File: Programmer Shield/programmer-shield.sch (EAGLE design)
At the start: 25 parts, among them T1 2N3904, T2 2N3904, T3 2N3904, T4 2N3904, U1 SPARK_CORECORE, U2 RELAYSONGLE, U3 RELAYSONGLE, U4 RELAYSONGLE, U5 RELAYSONGLE

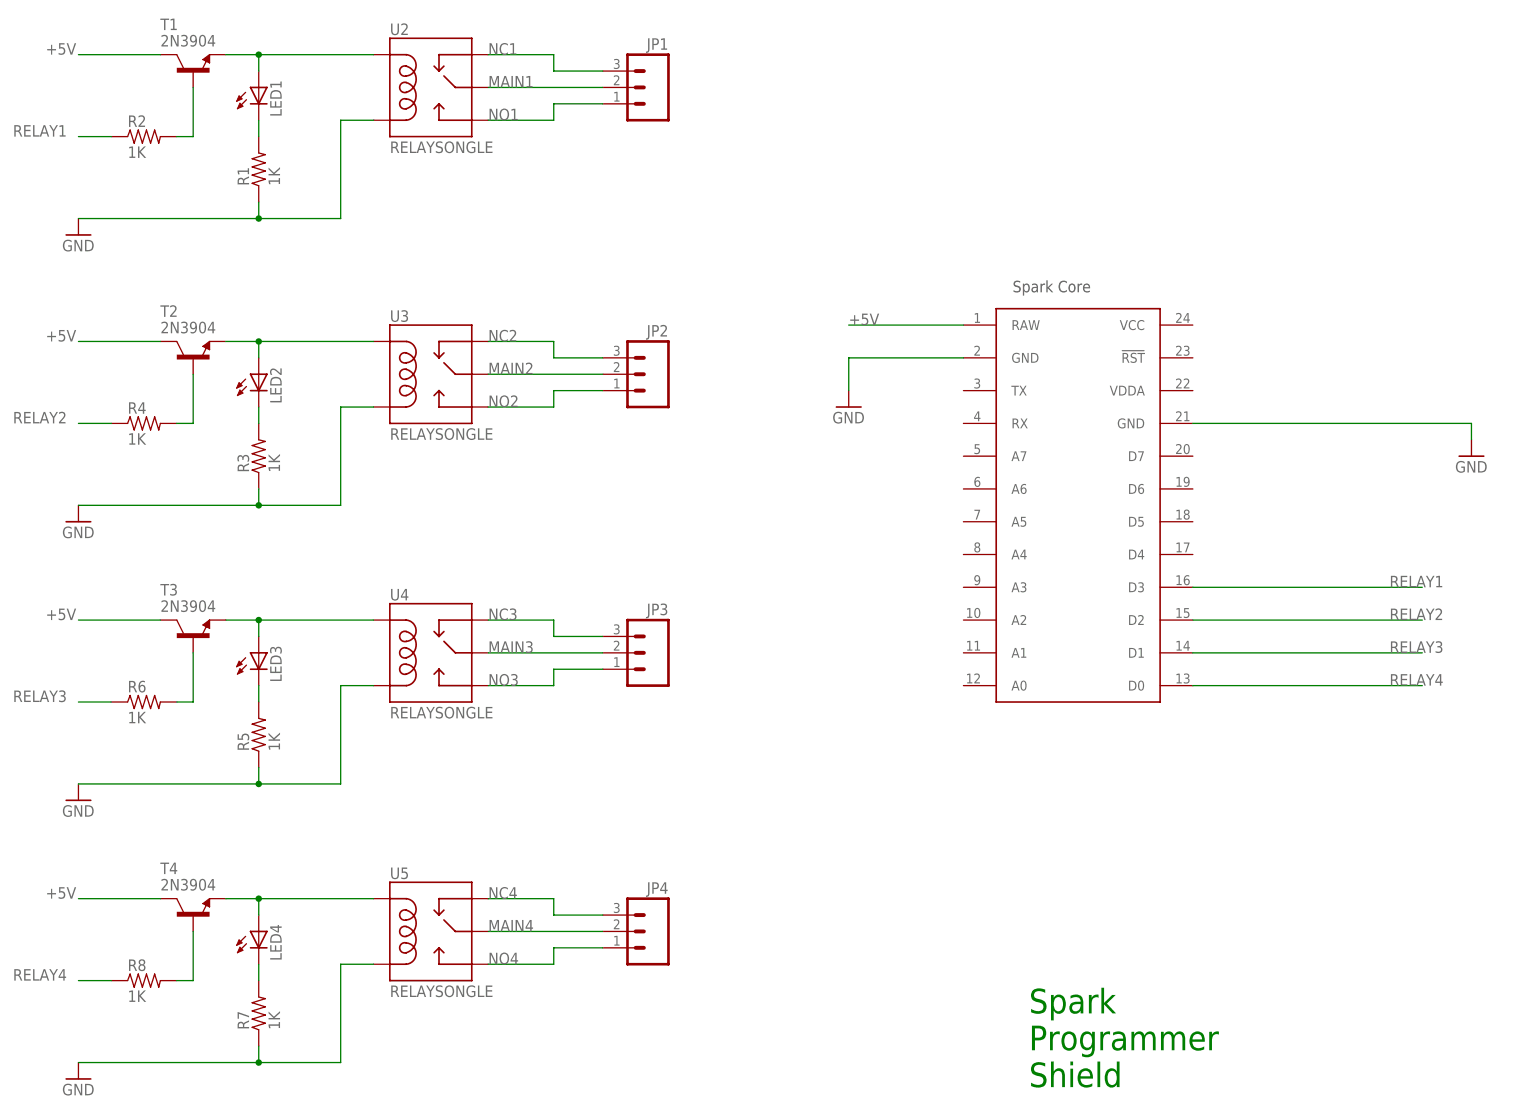
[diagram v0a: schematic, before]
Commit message: Fixed programmer shield
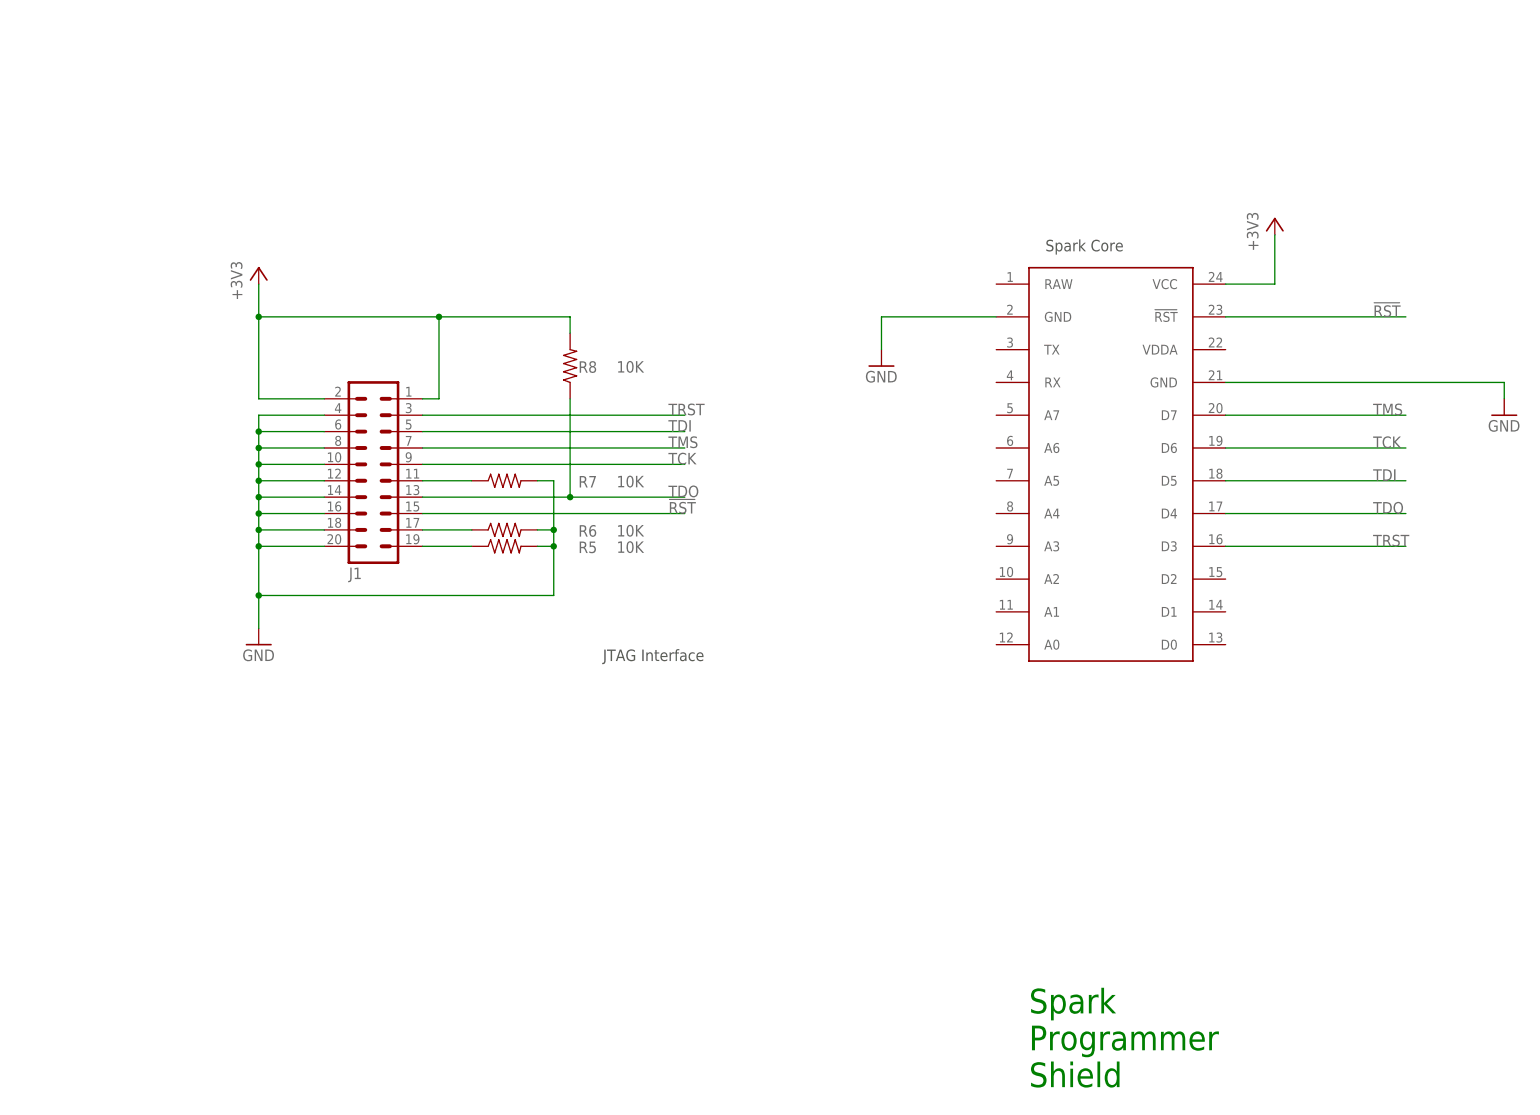
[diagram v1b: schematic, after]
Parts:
- removed JP1, JP2, JP3, JP4: (no value), SparkFun-Connectors:M03-SCREW-5MM
- removed LED1, LED2, LED3, LED4: (no value), SparkFun-LED:LED3MM
- removed R1, R2, R3, R4: 1K, SparkFun-Passives:RESISTORAXIAL-0.3
- removed T1, T2, T3, T4: 2N3904, transistor:2N3904
- removed U1: SPARK_CORECORE, Spark:SPARK_CORECORE
- removed U2, U3, U4, U5: RELAYSONGLE, Spark:RELAYSONGLE
- added J1: (no value), con-harting-ml:ML20
- added U$1: SPARK_CORECORE, Spark:SPARK_CORECORE
- R5, R6, R7, R8: value 1K -> 10K
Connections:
- removed net +5V: T1.C, T2.C, T3.C, T4.C, U1.RAW
- removed net MAIN1: JP1.2, U2.MAIN
- removed net MAIN2: JP2.2, U3.MAIN
- removed net MAIN3: JP3.2, U4.MAIN
- removed net MAIN4: JP4.2, U5.MAIN
- removed net N$1: LED1.A, T1.E, U2.COIL1
- removed net N$10: LED4.A, T4.E, U5.COIL1
- removed net N$11: R8.2, T4.B
- removed net N$12: LED4.C, R7.2
- removed net N$2: LED2.A, T2.E, U3.COIL1
- removed net N$3: R2.2, T1.B
- removed net N$4: LED1.C, R1.2
- removed net N$5: R4.2, T2.B
- removed net N$6: LED2.C, R3.2
- removed net N$7: LED3.A, T3.E, U4.COIL1
- removed net N$8: R6.2, T3.B
- removed net N$9: LED3.C, R5.2
- removed net NC1: JP1.3, U2.NC
- removed net NC2: JP2.3, U3.NC
- removed net NC3: JP3.3, U4.NC
- removed net NC4: JP4.3, U5.NC
- removed net NO1: JP1.1, U2.NO
- removed net NO2: JP2.1, U3.NO
- removed net NO3: JP3.1, U4.NO
- removed net NO4: JP4.1, U5.NO
- removed net RELAY1: R2.1, U1.D3
- removed net RELAY2: R4.1, U1.D2
- removed net RELAY3: R6.1, U1.D1
- removed net RELAY4: R8.1, U1.D0
- new net !RST: J1.15, U$1.!RST
- new net +3V3: J1.1, J1.2, R8.2, U$1.VCC
- new net N$13: J1.19, R5.1
- new net N$14: J1.17, R6.1
- new net N$15: J1.11, R7.1
- new net TCK: J1.9, U$1.D6
- new net TDI: J1.5, U$1.D5
- new net TDO: J1.13, R8.1, U$1.D4
- new net TMS: J1.7, U$1.D7
- new net TRST: J1.3, U$1.D3
- net GND: now also J1.10, J1.12, J1.14, J1.16, J1.18, J1.20, J1.4, J1.6, J1.8, R5.2, R6.2, R7.2, U$1.GND@2, U$1.GND@21; no longer R1.1, R3.1, R5.1, R7.1, U1.GND@2, U1.GND@21, U2.COIL2, U3.COIL2, U4.COIL2, U5.COIL2
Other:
- note added: "JTAG Interface"
- moved on the sheet: R5, R6, R7, R8

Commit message: Completed relay shield schematic and board
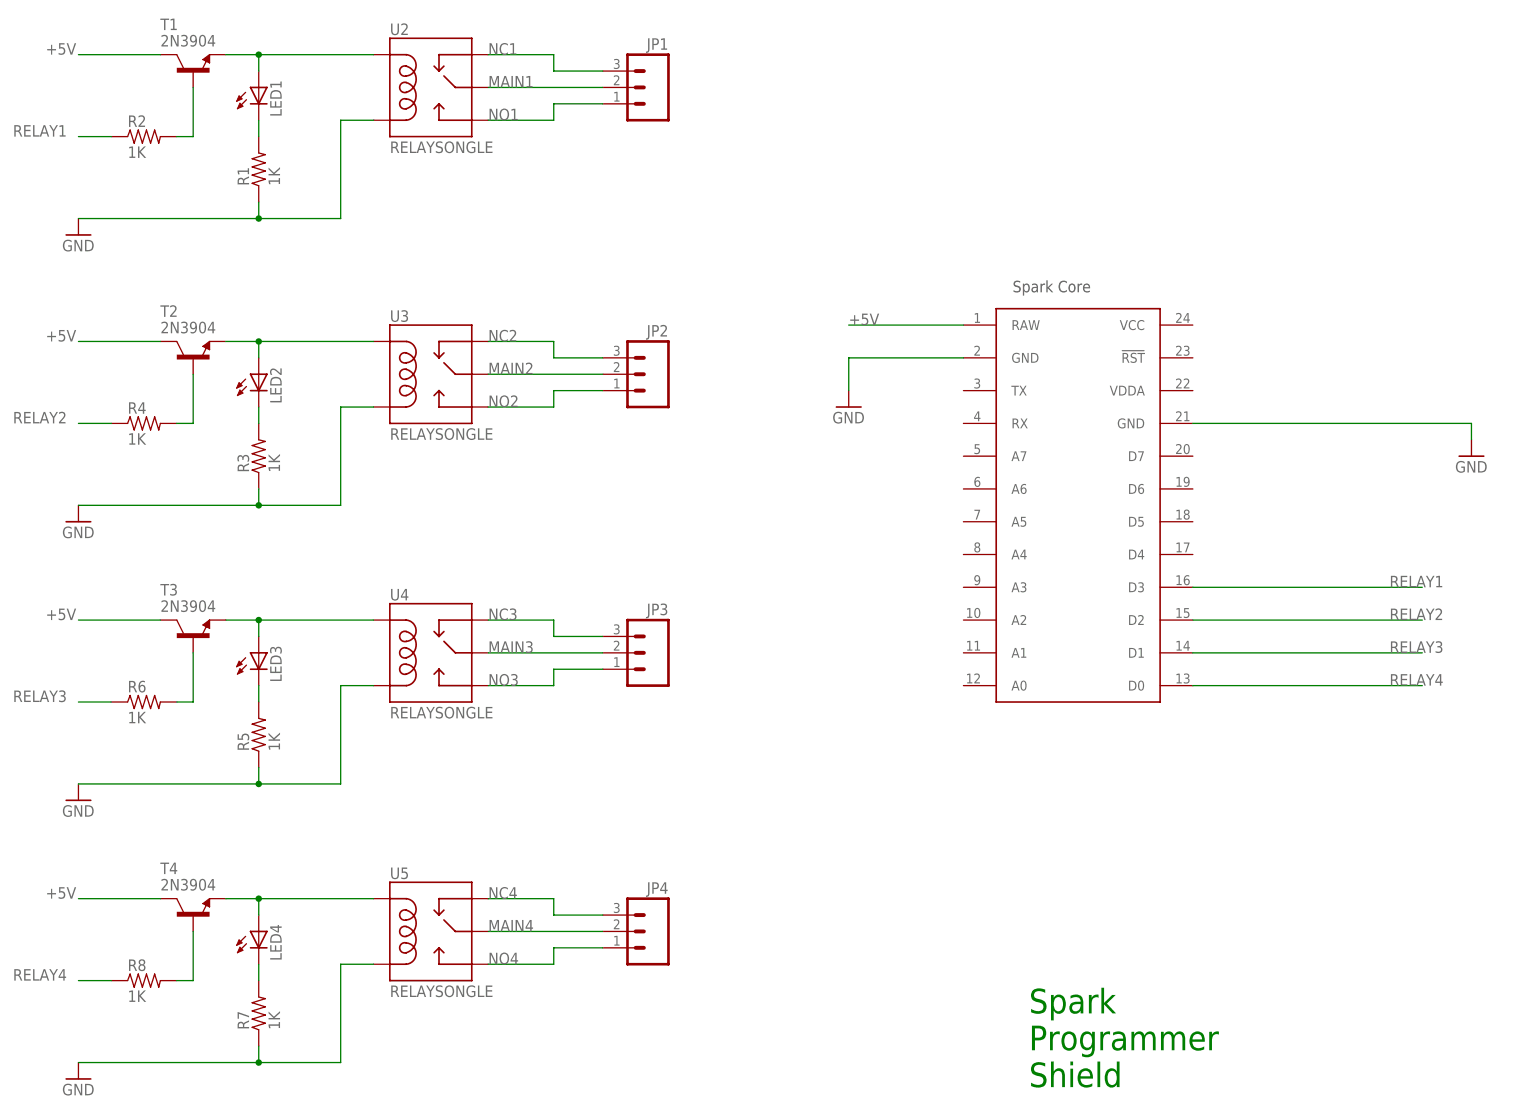
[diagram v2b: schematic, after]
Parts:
- removed J1: (no value), con-harting-ml:ML20
- removed U$1: SPARK_CORECORE, Spark:SPARK_CORECORE
- added JP1, JP2, JP3, JP4: (no value), SparkFun-Connectors:M03-SCREW-5MM
- added LED1, LED2, LED3, LED4: (no value), SparkFun-LED:LED3MM
- added R1, R2, R3, R4: 1K, SparkFun-Passives:RESISTORAXIAL-0.3
- added T1, T2, T3, T4: 2N3904, transistor:2N3904
- added U1: SPARK_CORECORE, Spark:SPARK_CORECORE
- added U2, U3, U4, U5: RELAYSONGLE, Spark:RELAYSONGLE
- R5, R6, R7, R8: value 10K -> 1K
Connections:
- removed net !RST: J1.15, U$1.!RST
- removed net +3V3: J1.1, J1.2, R8.2, U$1.VCC
- removed net N$13: J1.19, R5.1
- removed net N$14: J1.17, R6.1
- removed net N$15: J1.11, R7.1
- removed net TCK: J1.9, U$1.D6
- removed net TDI: J1.5, U$1.D5
- removed net TDO: J1.13, R8.1, U$1.D4
- removed net TMS: J1.7, U$1.D7
- removed net TRST: J1.3, U$1.D3
- new net +5V: T1.C, T2.C, T3.C, T4.C, U1.RAW
- new net MAIN1: JP1.2, U2.MAIN
- new net MAIN2: JP2.2, U3.MAIN
- new net MAIN3: JP3.2, U4.MAIN
- new net MAIN4: JP4.2, U5.MAIN
- new net N$1: LED1.A, T1.E, U2.COIL1
- new net N$10: LED4.A, T4.E, U5.COIL1
- new net N$11: R8.2, T4.B
- new net N$12: LED4.C, R7.2
- new net N$2: LED2.A, T2.E, U3.COIL1
- new net N$3: R2.2, T1.B
- new net N$4: LED1.C, R1.2
- new net N$5: R4.2, T2.B
- new net N$6: LED2.C, R3.2
- new net N$7: LED3.A, T3.E, U4.COIL1
- new net N$8: R6.2, T3.B
- new net N$9: LED3.C, R5.2
- new net NC1: JP1.3, U2.NC
- new net NC2: JP2.3, U3.NC
- new net NC3: JP3.3, U4.NC
- new net NC4: JP4.3, U5.NC
- new net NO1: JP1.1, U2.NO
- new net NO2: JP2.1, U3.NO
- new net NO3: JP3.1, U4.NO
- new net NO4: JP4.1, U5.NO
- new net RELAY1: R2.1, U1.D3
- new net RELAY2: R4.1, U1.D2
- new net RELAY3: R6.1, U1.D1
- new net RELAY4: R8.1, U1.D0
- net GND: now also R1.1, R3.1, R5.1, R7.1, U1.GND@2, U1.GND@21, U2.COIL2, U3.COIL2, U4.COIL2, U5.COIL2; no longer J1.10, J1.12, J1.14, J1.16, J1.18, J1.20, J1.4, J1.6, J1.8, R5.2, R6.2, R7.2, U$1.GND@2, U$1.GND@21
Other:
- note removed: "JTAG Interface"
- moved on the sheet: R5, R6, R7, R8
